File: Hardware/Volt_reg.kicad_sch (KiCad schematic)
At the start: 45 parts, among them Q2 BSZ025N04LS, Q3 BSZ025N04LS, Q4 BUK9M11-40EX, Q5 BUK9M11-40EX, U8 INA219AxDCN, U9 LM74810

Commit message: PCB mid design
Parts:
- C45: value C -> 10nF; footprint (none) -> Capacitor_SMD:C_0402_1005Metric
- C46, C54: footprint (none) -> Capacitor_SMD:C_0805_2012Metric
- C47: footprint (none) -> Capacitor_SMD:CP_Elec_10x10.5
- C48, C49: footprint (none) -> Capacitor_SMD:C_0402_1005Metric
- C50: value 4.7uf -> 4.7uF; footprint (none) -> Capacitor_SMD:C_0402_1005Metric
- C51, C52: value 0.1uf -> 0.1uF; footprint (none) -> Capacitor_SMD:C_0402_1005Metric
- C53: footprint (none) -> Capacitor_Tantalum_SMD:CP_EIA-7260-20_AVX-M
- L5: footprint (none) -> Inductor_SMD:L_10.4x10.4_H4.8
- R52: footprint (none) -> Resistor_SMD:R_0402_1005Metric
- U10: renamed from U?; footprint TPS552882QRPMRQ1 -> iclr:TPS552882QRPMRQ1
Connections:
- net AGND: no longer C29.2, C30.2, C32.2, C33.2, C46.2, C47.1, C53.2, C54.1, D7.2 (A2), Q4.1 (S), Q4.2 (S), Q4.3 (S), R31.2, R34.1, R47.2, U10.24 (PGND_2), U10.9 (PGND_1), U8.3 (GND), U8.7 (A0), U8.8 (A1), U9.7 (GND)
- new net GND: C29.2, C30.2, C32.2, C33.2, C46.2, C47.1, C53.2, C54.1, D7.2 (A2), Q4.1 (S), Q4.2 (S), Q4.3 (S), R31.2, R34.1, R47.2, U10.24 (PGND_2), U10.9 (PGND_1), U8.3 (GND), U8.7 (A0), U8.8 (A1), U9.7 (GND)
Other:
- moved on the sheet: R48
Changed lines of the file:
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@@
 	)
 	(junction
-		(at 69.85 176.53)
-		(diameter 0)
-		(color 0 0 0 0)
-	)
-	(junction
 		(at 204.47 72.39)
 		(diameter 0)
@@
 		(color 0 0 0 0)
 	)
-	(junction
-		(at 69.85 175.26)
-		(diameter 0)
-		(color 0 0 0 0)
-	)
 	(no_connect
 		(at 120.65 154.94)
@@
 	(wire
 		(pts
-			(xy 33.02 172.72) (xy 66.04 172.72)
+			(xy 33.02 172.72) (xy 59.69 172.72)
 		)
 		(stroke
@@
 	(wire
 		(pts
-			(xy 71.12 172.72) (xy 72.39 172.72)
+			(xy 64.77 172.72) (xy 72.39 172.72)
 		)
 		(stroke
@@
 	(wire
 		(pts
-			(xy 29.21 114.3) (xy 34.29 114.3)
-		)
-		(stroke
-			(width 0)
-			(type default)
-		)
-	)
-	(wire
-		(pts
 			(xy 57.15 160.02) (xy 72.39 160.02)
 		)
@@
 	(wire
 		(pts
-			(xy 69.85 175.26) (xy 72.39 175.26)
+			(xy 57.15 175.26) (xy 72.39 175.26)
 		)
 		(stroke
@@
 	(wire
 		(pts
-			(xy 69.85 176.53) (xy 69.85 175.26)
-		)
-		(stroke
-			(width 0)
-			(type default)
-		)
-	)
-	(wire
-		(pts
 			(xy 212.09 64.77) (xy 212.09 72.39)
 		)
@@
 	(wire
 		(pts
-			(xy 57.15 175.26) (xy 69.85 175.26)
-		)
-		(stroke
-			(width 0)
-			(type default)
-		)
-	)
-	(wire
-		(pts
 			(xy 48.26 156.21) (xy 48.26 153.67)
 		)
@@
 			)
 		)
-		(property "Value" "C"
-			(at 54.61 167.894 90)
+		(property "Value" "10nF"
+			(at 47.498 170.434 90)
 			(effects
 				(font
@@
 			)
 		)
-		(property "Footprint" ""
+		(property "Footprint" "Capacitor_SMD:C_0402_1005Metric"
 			(at 49.53 169.8752 0)
 			(effects
@@
 			)
 		)
-		(property "Value" "0.1uf"
+		(property "Value" "0.1uF"
 			(at 119.38 169.164 90)
 			(effects
@@
 			)
 		)
-		(property "Footprint" ""
+		(property "Footprint" "Capacitor_SMD:C_0402_1005Metric"
 			(at 121.92 171.1452 0)
 			(effects
@@
 			)
 		)
-		(property "Footprint" ""
+		(property "Footprint" "Capacitor_SMD:C_0805_2012Metric"
 			(at 38.4048 146.05 0)
 			(effects
@@
 		(lib_name "GND_1")
 		(lib_id "power:GND")
-		(at 29.21 114.3 0)
-		(unit 1)
-		(exclude_from_sim no)
-		(in_bom yes)
-		(on_board yes)
-		(dnp no)
-		(property "Reference" "#PWR076"
-			(at 29.21 120.65 0)
-			(effects
-				(font
-					(size 1.27 1.27)
-				)
-				(hide yes)
-			)
-		)
-		(property "Value" "GND"
-			(at 25.4 116.332 0)
-			(effects
-				(font
-					(size 1.27 1.27)
-				)
-			)
-		)
-		(property "Footprint" ""
-			(at 29.21 114.3 0)
-			(effects
-				(font
-					(size 1.27 1.27)
-				)
-				(hide yes)
-			)
-		)
-		(property "Datasheet" ""
-			(at 29.21 114.3 0)
-			(effects
-				(font
-					(size 1.27 1.27)
-				)
-				(hide yes)
-			)
-		)
-		(property "Description" "Power symbol creates a global label with name \"GND\" , ground"
-			(at 29.21 114.3 0)
-			(effects
-				(font
-					(size 1.27 1.27)
-				)
-				(hide yes)
-			)
-		)
-		(pin "1"
-		)
-		(instances
-			(project ""
-				(path "/7db990e4-92e1-4f99-b4d2-435bbec1ba83/ab7b921d-66d3-49d7-abff-63184671bf46"
-					(reference "#PWR076")
-					(unit 1)
-				)
-			)
-		)
-	)
-	(symbol
-		(lib_name "GND_1")
-		(lib_id "power:GND")
 		(at 46.99 173.99 0)
 		(unit 1)
@@
 			)
 		)
-		(property "Footprint" ""
+		(property "Footprint" "Capacitor_SMD:C_0402_1005Metric"
 			(at 152.4 155.9052 0)
 			(effects
@@
 			)
 		)
-		(property "Footprint" ""
+		(property "Footprint" "Capacitor_SMD:C_0805_2012Metric"
 			(at 56.1848 173.99 0)
 			(effects
@@
 			)
 		)
-		(property "Footprint" ""
+		(property "Footprint" "Resistor_SMD:R_0402_1005Metric"
 			(at 163.83 156.972 90)
 			(effects
@@
 			)
 		)
-		(property "Footprint" ""
+		(property "Footprint" "Capacitor_Tantalum_SMD:CP_EIA-7260-20_AVX-M"
 			(at 31.75 149.86 0)
 			(effects
@@
 			)
 		)
-		(property "Footprint" ""
+		(property "Footprint" "Capacitor_SMD:C_0402_1005Metric"
 			(at 144.78 159.7152 0)
 			(effects
@@
 	)
 	(symbol
-		(lib_name "GND_2")
-		(lib_id "power:GND")
-		(at 34.29 114.3 0)
-		(unit 1)
-		(exclude_from_sim no)
-		(in_bom yes)
-		(on_board yes)
-		(dnp no)
-		(property "Reference" "#PWR080"
-			(at 34.29 120.65 0)
-			(effects
-				(font
-					(size 1.27 1.27)
-				)
-				(hide yes)
-			)
-		)
-		(property "Value" "AGND"
-			(at 38.862 116.078 0)
-			(effects
-				(font
-					(size 1.27 1.27)
-				)
-			)
-		)
-		(property "Footprint" ""
-			(at 34.29 114.3 0)
-			(effects
-				(font
-					(size 1.27 1.27)
-				)
-				(hide yes)
-			)
-		)
-		(property "Datasheet" ""
-			(at 34.29 114.3 0)
-			(effects
-				(font
-					(size 1.27 1.27)
-				)
-				(hide yes)
-			)
-		)
-		(property "Description" "Power symbol creates a global label with name \"GND\" , ground"
-			(at 34.29 114.3 0)
-			(effects
-				(font
-					(size 1.27 1.27)
-				)
-				(hide yes)
-			)
-		)
-		(pin "1"
-		)
-		(instances
-			(project "Main board"
-				(path "/7db990e4-92e1-4f99-b4d2-435bbec1ba83/ab7b921d-66d3-49d7-abff-63184671bf46"
-					(reference "#PWR080")
-					(unit 1)
-				)
-			)
-		)
-	)
-	(symbol
 		(lib_id "Device:C_Small")
 		(at 110.49 57.15 0)
@@
 			)
 		)
-		(property "Value" "0.1uf"
+		(property "Value" "0.1uF"
 			(at 119.38 164.084 90)
 			(effects
@@
 			)
 		)
-		(property "Footprint" ""
+		(property "Footprint" "Capacitor_SMD:C_0402_1005Metric"
 			(at 121.92 166.0652 0)
 			(effects
@@
 			)
 		)
-		(property "Footprint" ""
+		(property "Footprint" "Inductor_SMD:L_10.4x10.4_H4.8"
 			(at 137.16 168.91 0)
 			(effects
@@
 	(symbol
 		(lib_id "Device:R_Small")
-		(at 68.58 172.72 270)
+		(at 62.23 172.72 270)
 		(unit 1)
 		(exclude_from_sim no)
@@
 		(dnp no)
 		(property "Reference" "R48"
-			(at 70.612 171.704 90)
+			(at 64.262 171.704 90)
 			(effects
 				(font
@@
 		)
 		(property "Value" "50k"
-			(at 63.246 171.704 90)
+			(at 56.896 171.704 90)
 			(effects
 				(font
@@
 		)
 		(property "Footprint" "Resistor_SMD:R_0402_1005Metric"
-			(at 68.58 172.72 0)
+			(at 62.23 172.72 0)
 			(effects
 				(font
@@
 		)
 		(property "Datasheet" "~"
-			(at 68.58 172.72 0)
+			(at 62.23 172.72 0)
 			(effects
 				(font
@@
 		)
 		(property "Description" "Resistor, small symbol"
-			(at 68.58 172.72 0)
+			(at 62.23 172.72 0)
 			(effects
 				(font
@@
 			)
 		)
-		(property "Footprint" ""
+		(property "Footprint" "Capacitor_SMD:CP_Elec_10x10.5"
 			(at 52.07 177.8 0)
 			(effects
@@
 			)
 		)
-		(property "Value" "4.7uf"
+		(property "Value" "4.7uF"
 			(at 134.62 161.544 90)
 			(effects
@@
 			)
 		)
-		(property "Footprint" ""
+		(property "Footprint" "Capacitor_SMD:C_0402_1005Metric"
 			(at 137.16 163.5252 0)
 			(effects
@@
 		(dnp no)
 		(fields_autoplaced yes)
-		(property "Reference" "U?"
+		(property "Reference" "U10"
 			(at 95.25 147.32 0)
 			(effects
@@
 			)
 		)
-		(property "Footprint" "TPS552882QRPMRQ1"
+		(property "Footprint" "iclr:TPS552882QRPMRQ1"
 			(at 114.3 249.86 0)
 			(effects
@@
 			(project ""
 				(path "/7db990e4-92e1-4f99-b4d2-435bbec1ba83/ab7b921d-66d3-49d7-abff-63184671bf46"
-					(reference "U?")
+					(reference "U10")
 					(unit 1)
 				)

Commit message: PCB done more ish
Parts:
- C47: footprint Capacitor_SMD:CP_Elec_10x10.5 -> Capacitor_Tantalum_SMD:CP_EIA-6032-28_Kemet-C
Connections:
- net AGND: now also R47.2
- net GND: no longer R47.2
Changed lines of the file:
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@@
 	)
 	(junction
-		(at 39.37 162.56)
-		(diameter 0)
-		(color 0 0 0 0)
-	)
-	(junction
 		(at 31.75 137.16)
 		(diameter 0)
@@
 	)
 	(junction
-		(at 44.45 162.56)
-		(diameter 0)
-		(color 0 0 0 0)
-	)
-	(junction
 		(at 101.6 54.61)
 		(diameter 0)
@@
 	)
 	(junction
+		(at 35.56 162.56)
+		(diameter 0)
+		(color 0 0 0 0)
+	)
+	(junction
 		(at 129.54 165.1)
 		(diameter 0)
@@
 	(wire
 		(pts
-			(xy 44.45 162.56) (xy 48.26 162.56)
-		)
-		(stroke
-			(width 0)
-			(type default)
-		)
-	)
-	(wire
-		(pts
 			(xy 233.68 82.55) (xy 233.68 86.36)
 		)
@@
 	(wire
 		(pts
-			(xy 39.37 162.56) (xy 44.45 162.56)
+			(xy 133.35 72.39) (xy 161.29 72.39)
 		)
 		(stroke
@@
 	(wire
 		(pts
-			(xy 133.35 72.39) (xy 161.29 72.39)
+			(xy 52.07 173.99) (xy 57.15 173.99)
 		)
 		(stroke
@@
 	(wire
 		(pts
-			(xy 52.07 173.99) (xy 57.15 173.99)
+			(xy 80.01 137.16) (xy 180.34 137.16)
 		)
 		(stroke
@@
 	(wire
 		(pts
-			(xy 80.01 137.16) (xy 180.34 137.16)
+			(xy 101.6 58.42) (xy 101.6 62.23)
 		)
 		(stroke
@@
 	(wire
 		(pts
-			(xy 101.6 58.42) (xy 101.6 62.23)
+			(xy 57.15 181.61) (xy 52.07 181.61)
 		)
 		(stroke
@@
 	(wire
 		(pts
-			(xy 57.15 181.61) (xy 52.07 181.61)
+			(xy 212.09 64.77) (xy 210.82 64.77)
 		)
 		(stroke
@@
 	(wire
 		(pts
-			(xy 212.09 64.77) (xy 210.82 64.77)
+			(xy 35.56 162.56) (xy 39.37 162.56)
 		)
 		(stroke
@@
 	(wire
 		(pts
-			(xy 31.75 162.56) (xy 39.37 162.56)
+			(xy 31.75 162.56) (xy 35.56 162.56)
 		)
 		(stroke
@@
 	)
 	(symbol
+		(lib_name "GND_1")
+		(lib_id "power:GND")
+		(at 35.56 162.56 0)
+		(unit 1)
+		(exclude_from_sim no)
+		(in_bom yes)
+		(on_board yes)
+		(dnp no)
+		(property "Reference" "#PWR078"
+			(at 35.56 168.91 0)
+			(effects
+				(font
+					(size 1.27 1.27)
+				)
+				(hide yes)
+			)
+		)
+		(property "Value" "GND"
+			(at 31.75 164.592 0)
+			(effects
+				(font
+					(size 1.27 1.27)
+				)
+			)
+		)
+		(property "Footprint" ""
+			(at 35.56 162.56 0)
+			(effects
+				(font
+					(size 1.27 1.27)
+				)
+				(hide yes)
+			)
+		)
+		(property "Datasheet" ""
+			(at 35.56 162.56 0)
+			(effects
+				(font
+					(size 1.27 1.27)
+				)
+				(hide yes)
+			)
+		)
+		(property "Description" "Power symbol creates a global label with name \"GND\" , ground"
+			(at 35.56 162.56 0)
+			(effects
+				(font
+					(size 1.27 1.27)
+				)
+				(hide yes)
+			)
+		)
+		(pin "1"
+		)
+		(instances
+			(project "Main board"
+				(path "/7db990e4-92e1-4f99-b4d2-435bbec1ba83/ab7b921d-66d3-49d7-abff-63184671bf46"
+					(reference "#PWR078")
+					(unit 1)
+				)
+			)
+		)
+	)
+	(symbol
 		(lib_id "Device:C")
 		(at 53.34 168.91 270)
@@
 	)
 	(symbol
+		(lib_name "GND_1")
+		(lib_id "power:GND")
+		(at 48.26 162.56 0)
+		(unit 1)
+		(exclude_from_sim no)
+		(in_bom yes)
+		(on_board yes)
+		(dnp no)
+		(property "Reference" "#PWR077"
+			(at 48.26 168.91 0)
+			(effects
+				(font
+					(size 1.27 1.27)
+				)
+				(hide yes)
+			)
+		)
+		(property "Value" "AGND"
+			(at 44.45 164.592 0)
+			(effects
+				(font
+					(size 1.27 1.27)
+				)
+			)
+		)
+		(property "Footprint" ""
+			(at 48.26 162.56 0)
+			(effects
+				(font
+					(size 1.27 1.27)
+				)
+				(hide yes)
+			)
+		)
+		(property "Datasheet" ""
+			(at 48.26 162.56 0)
+			(effects
+				(font
+					(size 1.27 1.27)
+				)
+				(hide yes)
+			)
+		)
+		(property "Description" "Power symbol creates a global label with name \"GND\" , ground"
+			(at 48.26 162.56 0)
+			(effects
+				(font
+					(size 1.27 1.27)
+				)
+				(hide yes)
+			)
+		)
+		(pin "1"
+		)
+		(instances
+			(project "Main board"
+				(path "/7db990e4-92e1-4f99-b4d2-435bbec1ba83/ab7b921d-66d3-49d7-abff-63184671bf46"
+					(reference "#PWR077")
+					(unit 1)
+				)
+			)
+		)
+	)
+	(symbol
 		(lib_id "Connector:TestPoint")
 		(at 214.63 109.22 270)
@@
 			)
 		)
-		(property "Footprint" "Capacitor_SMD:CP_Elec_10x10.5"
+		(property "Footprint" "Capacitor_Tantalum_SMD:CP_EIA-6032-28_Kemet-C"
 			(at 52.07 177.8 0)
 			(effects
@@
 					(unit 1)
 				)
-			)
-		)
-	)
-	(symbol
-		(lib_name "GND_1")
-		(lib_id "power:GND")
-		(at 44.45 162.56 0)
-		(unit 1)
-		(exclude_from_sim no)
-		(in_bom yes)
-		(on_board yes)
-		(dnp no)
-		(property "Reference" "#PWR090"
-			(at 44.45 168.91 0)
-			(effects
-				(font
-					(size 1.27 1.27)
-				)
-				(hide yes)
-			)
-		)
-		(property "Value" "GND"
-			(at 40.64 164.592 0)
-			(effects
-				(font
-					(size 1.27 1.27)
-				)
-			)
-		)
-		(property "Footprint" ""
-			(at 44.45 162.56 0)
-			(effects
-				(font
-					(size 1.27 1.27)
-				)
-				(hide yes)
-			)
-		)
-		(property "Datasheet" ""
-			(at 44.45 162.56 0)
-			(effects
-				(font
-					(size 1.27 1.27)
-				)
-				(hide yes)
-			)
-		)
-		(property "Description" "Power symbol creates a global label with name \"GND\" , ground"
-			(at 44.45 162.56 0)
-			(effects
-				(font
-					(size 1.27 1.27)
-				)
-				(hide yes)
-			)
-		)
-		(pin "1"
-		)
-		(instances
-			(project "Main board"
-				(path "/7db990e4-92e1-4f99-b4d2-435bbec1ba83/ab7b921d-66d3-49d7-abff-63184671bf46"
-					(reference "#PWR090")
-					(unit 1)
-				)

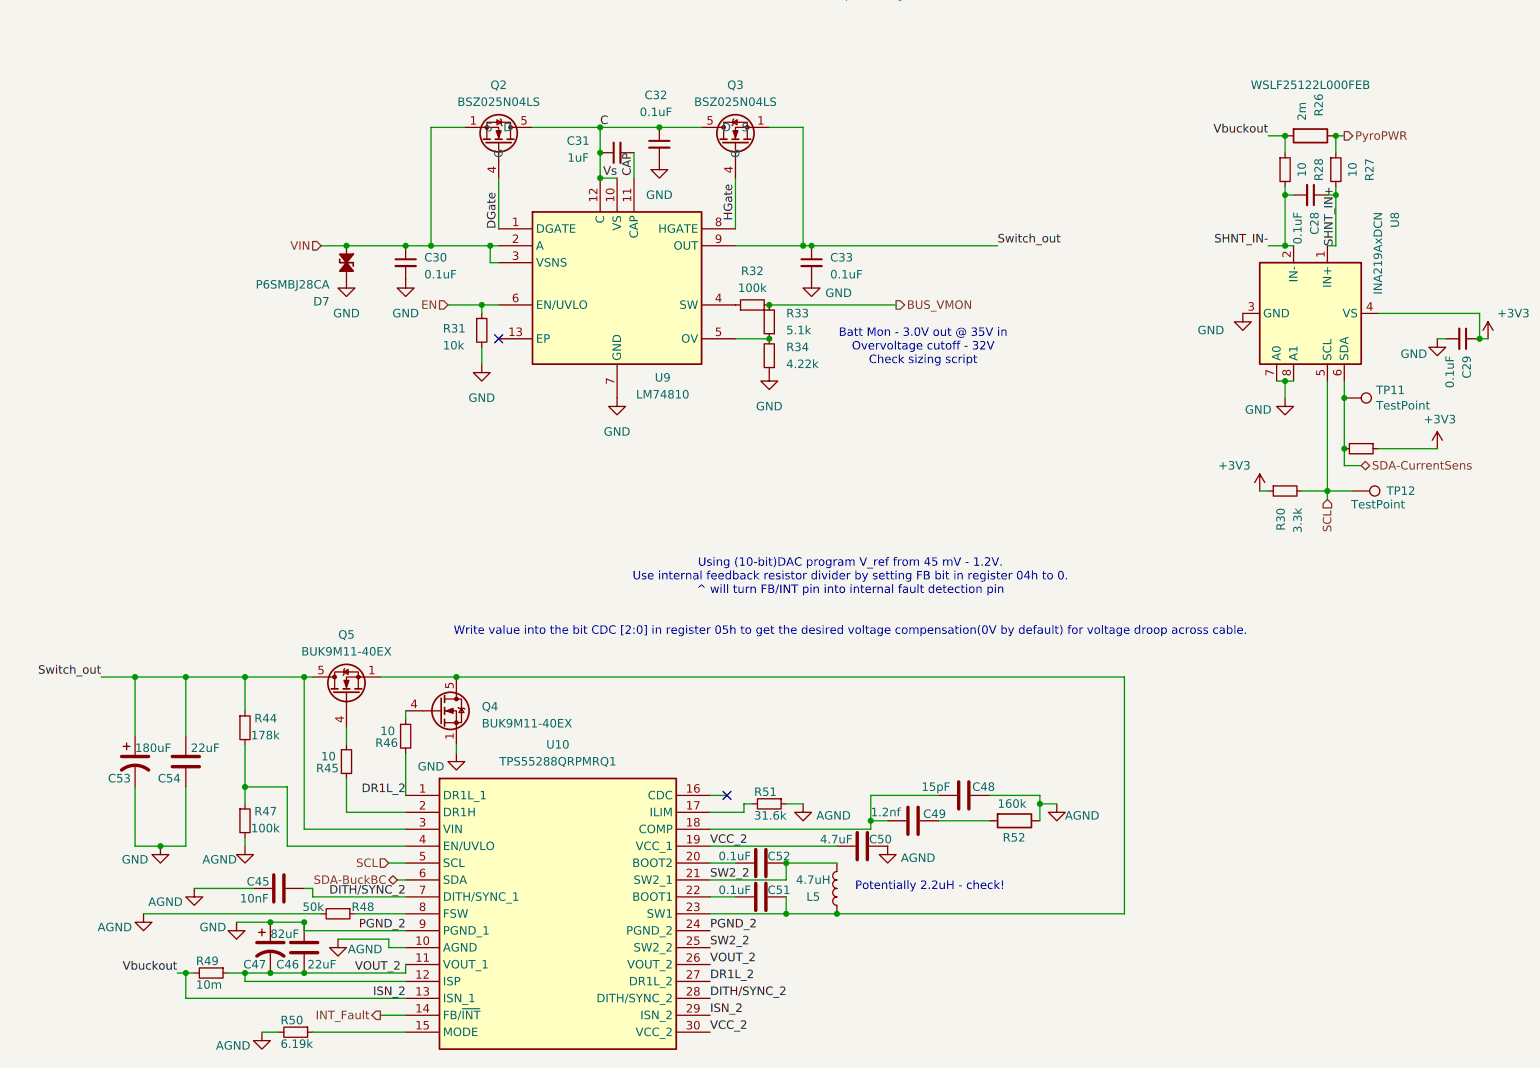
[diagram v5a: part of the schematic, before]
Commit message: Crosshair V1.0
New pyro connectors, silkscreen sorted, mostly connected properly + cool new name and image
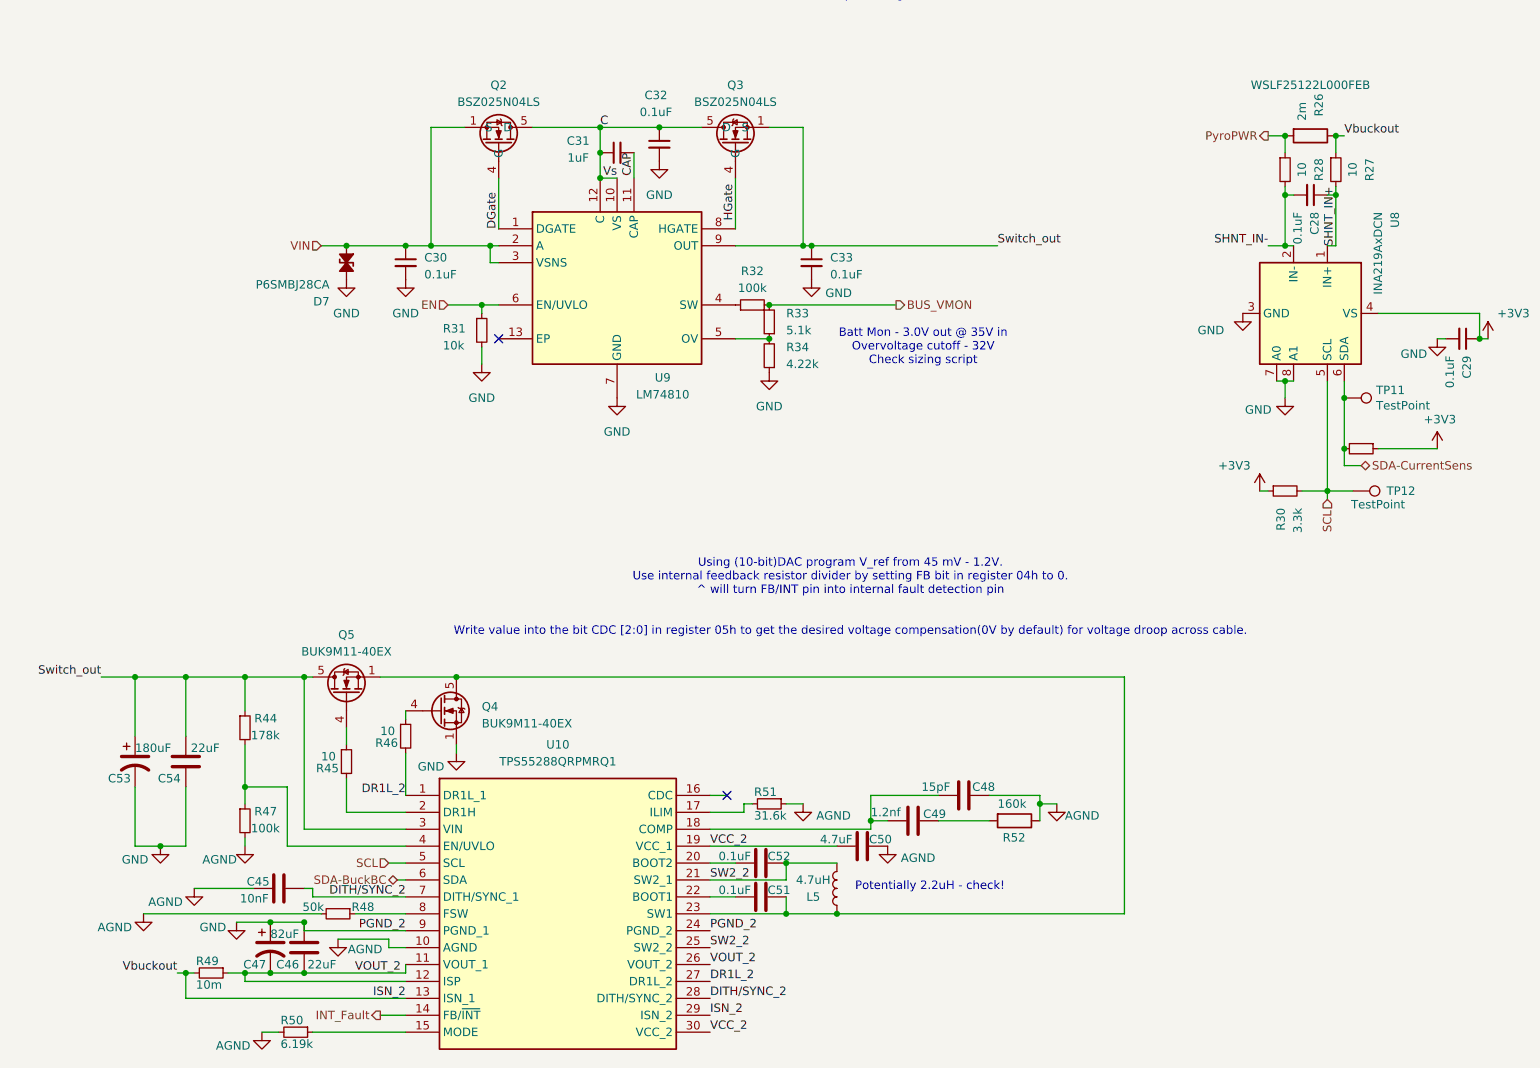
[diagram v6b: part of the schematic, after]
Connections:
- net ISN_2: now also R26.1, R27.1; no longer R26.2, R28.1
- net PyroPWR: now also R26.2, R28.1; no longer R26.1, R27.1
